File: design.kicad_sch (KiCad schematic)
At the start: 178 parts, among them J1 TYPE-C-31-M-12, U1 TTP223, U10 ATtiny1616-S, U2 TTP223, U3 TTP223, U4 TTP223, U5 TTP223, U6 TTP223, U7 TTP223, U8 TTP223, U9 MAX77751CEFG_T

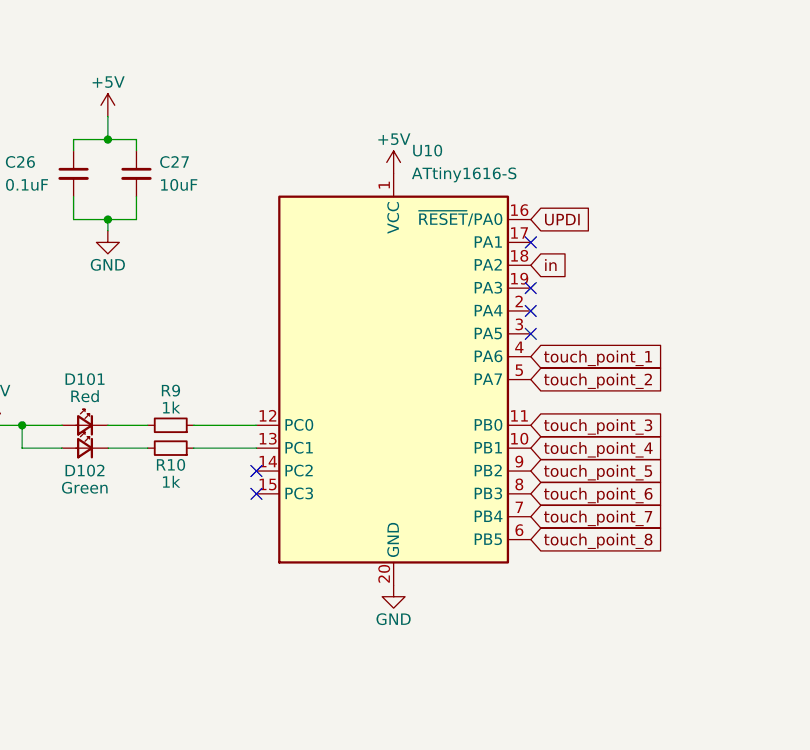
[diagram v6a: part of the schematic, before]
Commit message: change to QFN 1616
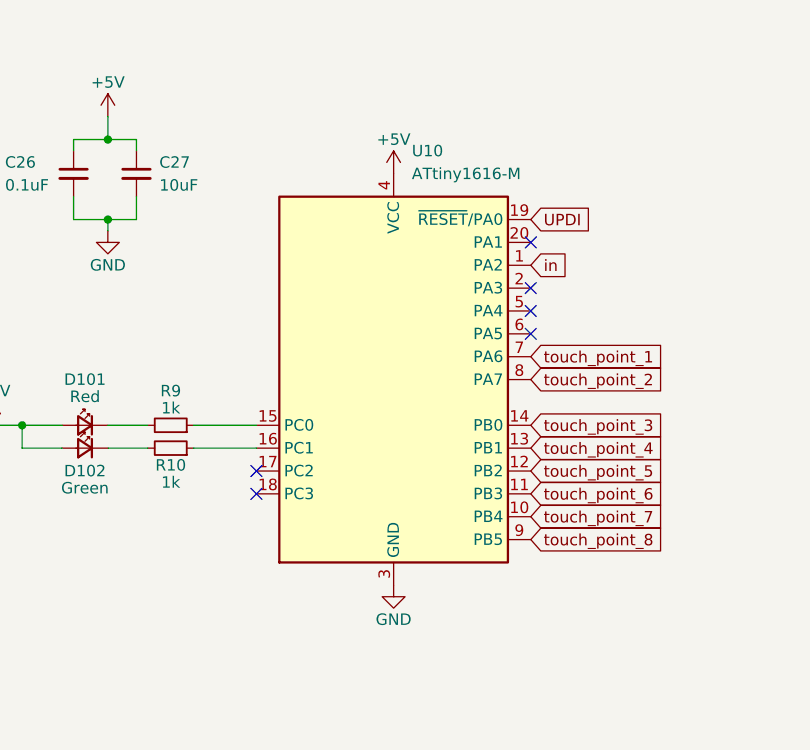
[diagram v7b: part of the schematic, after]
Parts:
- removed U10: ATtiny1616-S, Package_SO:SOIC-20W_7.5x12.8mm_P1.27mm, symbol MCU_Microchip_ATtiny:ATtiny1616-S
- added U10: ATtiny1616-M, Package_DFN_QFN:VQFN-20-1EP_3x3mm_P0.4mm_EP1.7x1.7mm, symbol MCU_Microchip_ATtiny:ATtiny1616-M
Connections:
- net +5V: now also U10.4 (VCC)
- net GND: now also U10.21 (GND), U10.3 (GND)
- net UPDI: now also U10.19 (~{RESET}/PA0)
- net in: now also U10.1 (PA2)
- net touch_point_1: now also U10.7 (PA6)
- net touch_point_2: now also U10.8 (PA7)
- net touch_point_3: now also U10.14 (PB0)
- net touch_point_4: now also U10.13 (PB1)
- net touch_point_5: now also U10.12 (PB2)
- net touch_point_6: now also U10.11 (PB3)
- net touch_point_7: now also U10.10 (PB4)
- net touch_point_8: now also U10.9 (PB5)
- net at R9.1: now also U10.15 (PC0)
- net at R10.1: now also U10.16 (PC1)
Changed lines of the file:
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@@
     (pin "1")
   )
+  (symbol (lib_id "MCU_Microchip_ATtiny:ATtiny1616-M") (at 385.445 314.96 0) (unit 1)
+    (in_bom yes) (on_board yes) (fields_autoplaced)
+    (property "Reference" "U10" (id 0) (at 387.4644 289.56 0)
+      (effects (font (size 1.27 1.27)) (justify left))
+    )
+    (property "Value" "ATtiny1616-M" (id 1) (at 387.4644 292.1 0)
+      (effects (font (size 1.27 1.27)) (justify left))
+    )
+    (property "Footprint" "Package_DFN_QFN:VQFN-20-1EP_3x3mm_P0.4mm_EP1.7x1.7mm" (id 2) (at 385.445 314.96 0)
+      (effects (font (size 1.27 1.27) italic) hide)
+    )
+    (property "Datasheet" "http://ww1.microchip.com/downloads/en/DeviceDoc/ATtiny3216_ATtiny1616-data-sheet-40001997B.pdf" (id 3) (at 385.445 314.96 0)
+      (effects (font (size 1.27 1.27)) hide)
+    )
+    (pin "1")
+    (pin "10")
+    (pin "11")
+    (pin "12")
+    (pin "13")
+    (pin "14")
+    (pin "15")
+    (pin "16")
+    (pin "17")
+    (pin "18")
+    (pin "19")
+    (pin "2")
+    (pin "20")
+    (pin "21")
+    (pin "3")
+    (pin "4")
+    (pin "5")
+    (pin "6")
+    (pin "7")
+    (pin "8")
+    (pin "9")
+  )
   (symbol (lib_id "power:GND") (at 485.14 153.67 0) (unit 1)
     (in_bom yes) (on_board yes)
@@
     (pin "4")
   )
-  (symbol (lib_id "MCU_Microchip_ATtiny:ATtiny1616-S") (at 385.445 314.96 0) (unit 1)
-    (in_bom yes) (on_board yes) (fields_autoplaced)
-    (property "Reference" "U10" (id 0) (at 387.4644 289.56 0)
-      (effects (font (size 1.27 1.27)) (justify left))
-    )
-    (property "Value" "ATtiny1616-S" (id 1) (at 387.4644 292.1 0)
-      (effects (font (size 1.27 1.27)) (justify left))
-    )
-    (property "Footprint" "Package_SO:SOIC-20W_7.5x12.8mm_P1.27mm" (id 2) (at 385.445 314.96 0)
-      (effects (font (size 1.27 1.27) italic) hide)
-    )
-    (property "Datasheet" "http://ww1.microchip.com/downloads/en/DeviceDoc/ATtiny3216_ATtiny1616-data-sheet-40001997B.pdf" (id 3) (at 385.445 314.96 0)
-      (effects (font (size 1.27 1.27)) hide)
-    )
-    (pin "1")
-    (pin "10")
-    (pin "11")
-    (pin "12")
-    (pin "13")
-    (pin "14")
-    (pin "15")
-    (pin "16")
-    (pin "17")
-    (pin "18")
-    (pin "19")
-    (pin "2")
-    (pin "20")
-    (pin "3")
-    (pin "4")
-    (pin "5")
-    (pin "6")
-    (pin "7")
-    (pin "8")
-    (pin "9")
-  )
   (symbol (lib_id "power:GND") (at 551.18 153.67 0) (unit 1)
     (in_bom yes) (on_board yes)
@@
   (symbol (lib_id "power:+5V") (at 196.215 118.11 0) (unit 1)
     (in_bom yes) (on_board yes)
-    (property "Reference" "#PWR?" (id 0) (at 196.215 121.92 0)
+    (property "Reference" "#PWR0256" (id 0) (at 196.215 121.92 0)
       (effects (font (size 1.27 1.27)) hide)
     )
@@
     )
     (path "/e1406b4f-a2c2-4e53-8d5b-e22f2d83d6a5"
-      (reference "#PWR?") (unit 1) (value "+5V") (footprint "")
+      (reference "#PWR0256") (unit 1) (value "+5V") (footprint "")
     )
     (path "/07d1a4e0-733f-4ad9-a5c8-74465e2c313d"
@@
       (reference "U9") (unit 1) (value "MAX77751CEFG_T") (footprint "Snapeda:IC_MAX77751CEFG_T")
     )
-    (path "/a71cdeed-1051-4d62-bd94-dca0a19008a3"
-      (reference "U10") (unit 1) (value "ATtiny1616-S") (footprint "Package_SO:SOIC-20W_7.5x12.8mm_P1.27mm")
+    (path "/06824c68-cecd-4391-bdbb-9ca63f76c08e"
+      (reference "U10") (unit 1) (value "ATtiny1616-M") (footprint "Package_DFN_QFN:VQFN-20-1EP_3x3mm_P0.4mm_EP1.7x1.7mm")
     )
   )

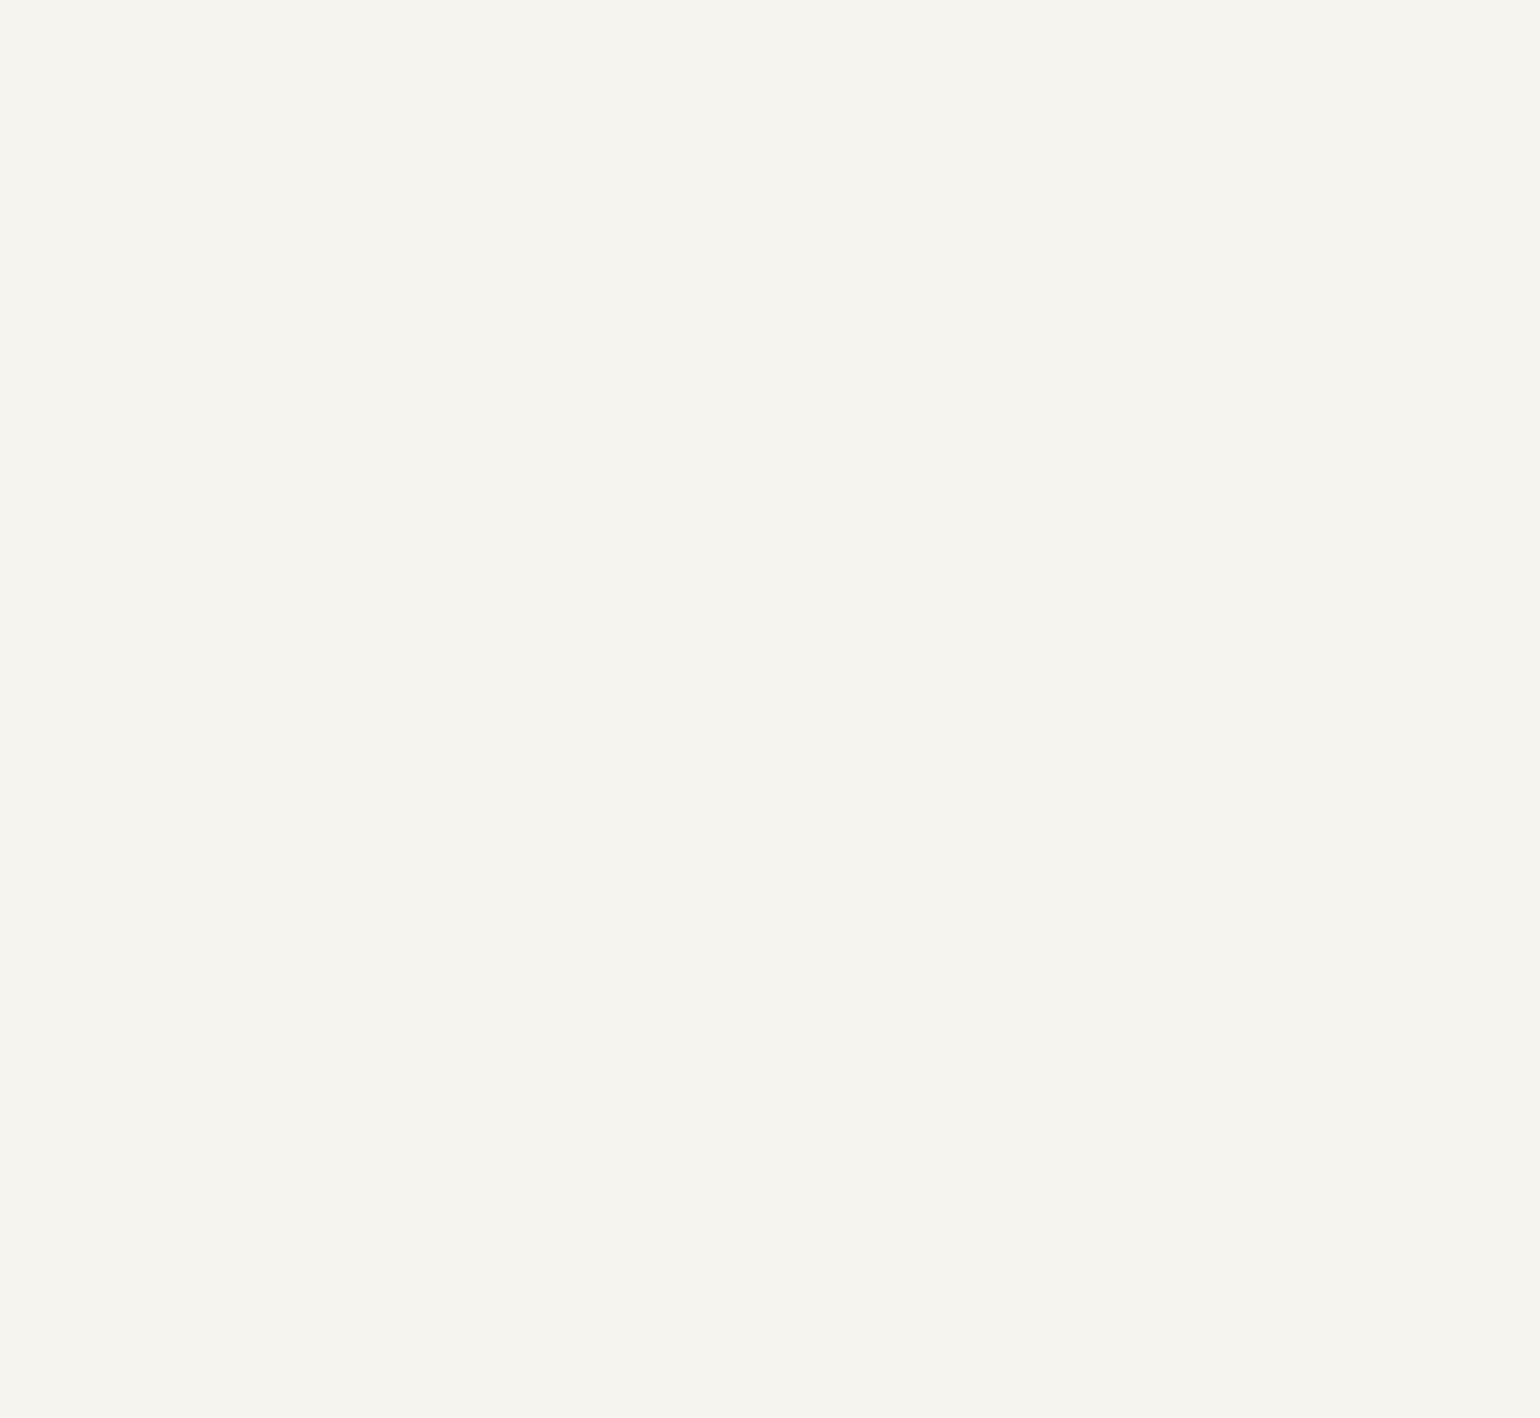
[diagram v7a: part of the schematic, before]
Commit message: some confusing LED double footprints
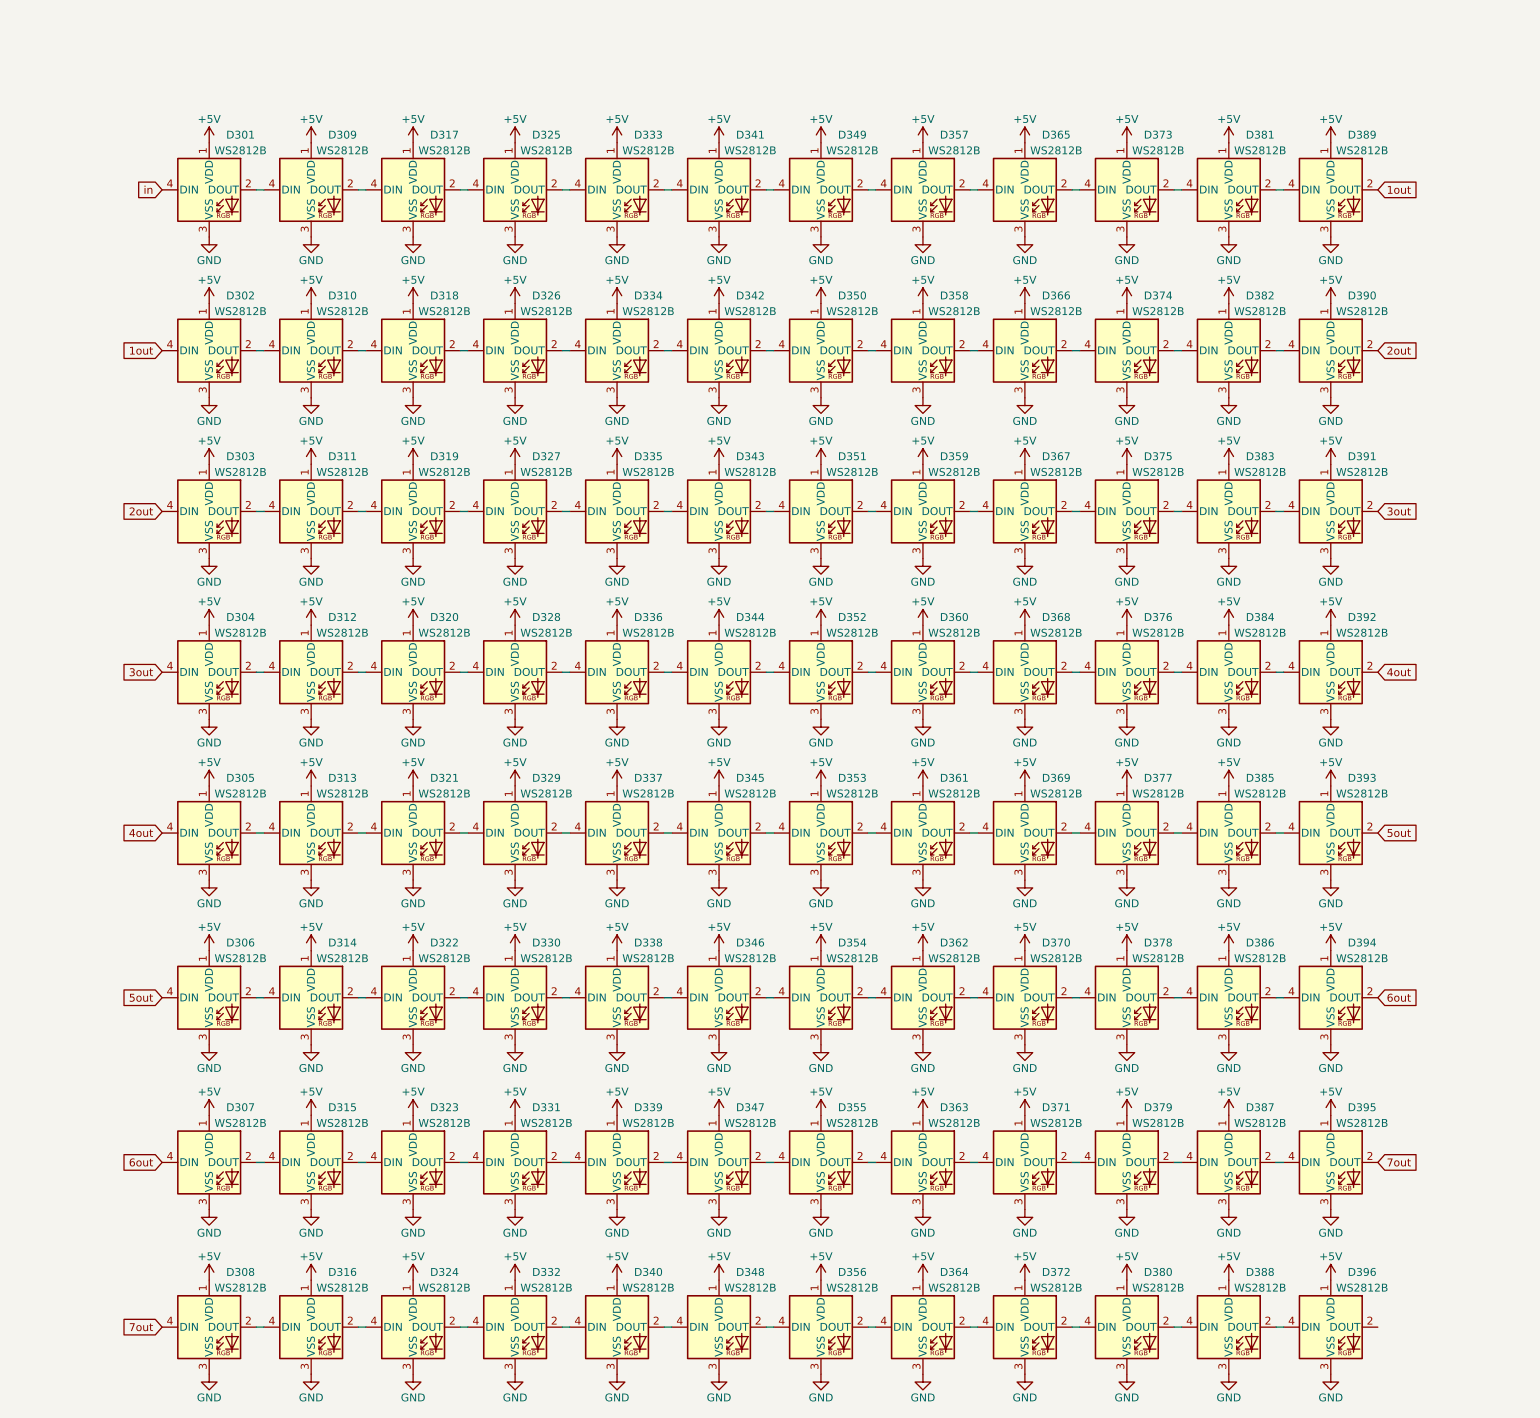
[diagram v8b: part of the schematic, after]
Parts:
- added D301, D302, D303, D304, D305, D306, D307, D308, D309, D310, D311, D312, D313, D314, D315, D316, D317, D318, D319, D320, D321, D322, D323, D324, D325, D326, D327, D328, D329, D330, D331, D332, D333, D334, D335, D336, D337, D338, D339, D340, D341, D342, D343, D344, D345, D346, D347, D348, D349, D350, D351, D352, D353, D354, D355, D356, D357, D358, D359, D360, D361, D362, D363, D364, D365, D366, D367, D368, D369, D370, D371, D372, D373, D374, D375, D376, D377, D378, D379, D380, D381, D382, D383, D384, D385, D386, D387, D388, D389, D390, D391, D392, D393, D394, D395, D396: WS2812B, LED_SMD:LED_WS2812B_PLCC4_5.0x5.0mm_P3.2mm, symbol LED:WS2812B
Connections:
- net +5V: now also D301.1 (VDD), D302.1 (VDD), D303.1 (VDD), D304.1 (VDD), D305.1 (VDD), D306.1 (VDD), D307.1 (VDD), D308.1 (VDD), D309.1 (VDD), D310.1 (VDD), D311.1 (VDD), D312.1 (VDD), D313.1 (VDD), D314.1 (VDD), D315.1 (VDD), D316.1 (VDD), D317.1 (VDD), D318.1 (VDD), D319.1 (VDD), D320.1 (VDD), D321.1 (VDD), D322.1 (VDD), D323.1 (VDD), D324.1 (VDD), D325.1 (VDD), D326.1 (VDD), D327.1 (VDD), D328.1 (VDD), D329.1 (VDD), D330.1 (VDD), D331.1 (VDD), D332.1 (VDD), D333.1 (VDD), D334.1 (VDD), D335.1 (VDD), D336.1 (VDD), D337.1 (VDD), D338.1 (VDD), D339.1 (VDD), D340.1 (VDD), D341.1 (VDD), D342.1 (VDD), D343.1 (VDD), D344.1 (VDD), D345.1 (VDD), D346.1 (VDD), D347.1 (VDD), D348.1 (VDD), D349.1 (VDD), D350.1 (VDD), D351.1 (VDD), D352.1 (VDD), D353.1 (VDD), D354.1 (VDD), D355.1 (VDD), D356.1 (VDD), D357.1 (VDD), D358.1 (VDD), D359.1 (VDD), D360.1 (VDD), D361.1 (VDD), D362.1 (VDD), D363.1 (VDD), D364.1 (VDD), D365.1 (VDD), D366.1 (VDD), D367.1 (VDD), D368.1 (VDD), D369.1 (VDD), D370.1 (VDD), D371.1 (VDD), D372.1 (VDD), D373.1 (VDD), D374.1 (VDD), D375.1 (VDD), D376.1 (VDD), D377.1 (VDD), D378.1 (VDD), D379.1 (VDD), D380.1 (VDD), D381.1 (VDD), D382.1 (VDD), D383.1 (VDD), D384.1 (VDD), D385.1 (VDD), D386.1 (VDD), D387.1 (VDD), D388.1 (VDD), D389.1 (VDD), D390.1 (VDD), D391.1 (VDD), D392.1 (VDD), D393.1 (VDD), D394.1 (VDD), D395.1 (VDD), D396.1 (VDD)
- net 1out: now also D302.4 (DIN), D389.2 (DOUT)
- net 2out: now also D303.4 (DIN), D390.2 (DOUT)
- net 3out: now also D304.4 (DIN), D391.2 (DOUT)
- net 4out: now also D305.4 (DIN), D392.2 (DOUT)
- net 5out: now also D306.4 (DIN), D393.2 (DOUT)
- net 6out: now also D307.4 (DIN), D394.2 (DOUT)
- net 7out: now also D308.4 (DIN), D395.2 (DOUT)
- net GND: now also D301.3 (VSS), D302.3 (VSS), D303.3 (VSS), D304.3 (VSS), D305.3 (VSS), D306.3 (VSS), D307.3 (VSS), D308.3 (VSS), D309.3 (VSS), D310.3 (VSS), D311.3 (VSS), D312.3 (VSS), D313.3 (VSS), D314.3 (VSS), D315.3 (VSS), D316.3 (VSS), D317.3 (VSS), D318.3 (VSS), D319.3 (VSS), D320.3 (VSS), D321.3 (VSS), D322.3 (VSS), D323.3 (VSS), D324.3 (VSS), D325.3 (VSS), D326.3 (VSS), D327.3 (VSS), D328.3 (VSS), D329.3 (VSS), D330.3 (VSS), D331.3 (VSS), D332.3 (VSS), D333.3 (VSS), D334.3 (VSS), D335.3 (VSS), D336.3 (VSS), D337.3 (VSS), D338.3 (VSS), D339.3 (VSS), D340.3 (VSS), D341.3 (VSS), D342.3 (VSS), D343.3 (VSS), D344.3 (VSS), D345.3 (VSS), D346.3 (VSS), D347.3 (VSS), D348.3 (VSS), D349.3 (VSS), D350.3 (VSS), D351.3 (VSS), D352.3 (VSS), D353.3 (VSS), D354.3 (VSS), D355.3 (VSS), D356.3 (VSS), D357.3 (VSS), D358.3 (VSS), D359.3 (VSS), D360.3 (VSS), D361.3 (VSS), D362.3 (VSS), D363.3 (VSS), D364.3 (VSS), D365.3 (VSS), D366.3 (VSS), D367.3 (VSS), D368.3 (VSS), D369.3 (VSS), D370.3 (VSS), D371.3 (VSS), D372.3 (VSS), D373.3 (VSS), D374.3 (VSS), D375.3 (VSS), D376.3 (VSS), D377.3 (VSS), D378.3 (VSS), D379.3 (VSS), D380.3 (VSS), D381.3 (VSS), D382.3 (VSS), D383.3 (VSS), D384.3 (VSS), D385.3 (VSS), D386.3 (VSS), D387.3 (VSS), D388.3 (VSS), D389.3 (VSS), D390.3 (VSS), D391.3 (VSS), D392.3 (VSS), D393.3 (VSS), D394.3 (VSS), D395.3 (VSS), D396.3 (VSS)
- net in: now also D301.4 (DIN)
- new net: D367.2 (DOUT), D375.4 (DIN)
- new net: D359.2 (DOUT), D367.4 (DIN)
- new net: D332.2 (DOUT), D340.4 (DIN)
- new net: D324.2 (DOUT), D332.4 (DIN)
- new net: D327.2 (DOUT), D335.4 (DIN)
- new net: D319.2 (DOUT), D327.4 (DIN)
- new net: D302.2 (DOUT), D310.4 (DIN)
- new net: D328.2 (DOUT), D336.4 (DIN)
- new net: D320.2 (DOUT), D328.4 (DIN)
- new net: D352.2 (DOUT), D360.4 (DIN)
- new net: D344.2 (DOUT), D352.4 (DIN)
- new net: D375.2 (DOUT), D383.4 (DIN)
- new net: D351.2 (DOUT), D359.4 (DIN)
- new net: D305.2 (DOUT), D313.4 (DIN)
- new net: D360.2 (DOUT), D368.4 (DIN)
- new net: D338.2 (DOUT), D346.4 (DIN)
- new net: D330.2 (DOUT), D338.4 (DIN)
- new net: D311.2 (DOUT), D319.4 (DIN)
- new net: D303.2 (DOUT), D311.4 (DIN)
- new net: D333.2 (DOUT), D341.4 (DIN)
- new net: D325.2 (DOUT), D333.4 (DIN)
- new net: D343.2 (DOUT), D351.4 (DIN)
- new net: D335.2 (DOUT), D343.4 (DIN)
- new net: D301.2 (DOUT), D309.4 (DIN)
- new net: D384.2 (DOUT), D392.4 (DIN)
- new net: D376.2 (DOUT), D384.4 (DIN)
- new net: D365.2 (DOUT), D373.4 (DIN)
- new net: D357.2 (DOUT), D365.4 (DIN)
- new net: D354.2 (DOUT), D362.4 (DIN)
- new net: D346.2 (DOUT), D354.4 (DIN)
- new net: D339.2 (DOUT), D347.4 (DIN)
- new net: D331.2 (DOUT), D339.4 (DIN)
- new net: D345.2 (DOUT), D353.4 (DIN)
- new net: D337.2 (DOUT), D345.4 (DIN)
- new net: D386.2 (DOUT), D394.4 (DIN)
- new net: D316.2 (DOUT), D324.4 (DIN)
- new net: D315.2 (DOUT), D323.4 (DIN)
- new net: D307.2 (DOUT), D315.4 (DIN)
- new net: D382.2 (DOUT), D390.4 (DIN)
- new net: D374.2 (DOUT), D382.4 (DIN)
- new net: D387.2 (DOUT), D395.4 (DIN)
- new net: D379.2 (DOUT), D387.4 (DIN)
- new net: D361.2 (DOUT), D369.4 (DIN)
- new net: D353.2 (DOUT), D361.4 (DIN)
- new net: D329.2 (DOUT), D337.4 (DIN)
- new net: D321.2 (DOUT), D329.4 (DIN)
- new net: D378.2 (DOUT), D386.4 (DIN)
- new net: D370.2 (DOUT), D378.4 (DIN)
- new net: D334.2 (DOUT), D342.4 (DIN)
- new net: D326.2 (DOUT), D334.4 (DIN)
- new net: D364.2 (DOUT), D372.4 (DIN)
- new net: D356.2 (DOUT), D364.4 (DIN)
- new net: D385.2 (DOUT), D393.4 (DIN)
- new net: D377.2 (DOUT), D385.4 (DIN)
- new net: D308.2 (DOUT), D316.4 (DIN)
- new net: D383.2 (DOUT), D391.4 (DIN)
- new net: D373.2 (DOUT), D381.4 (DIN)
- new net: D380.2 (DOUT), D388.4 (DIN)
- new net: D372.2 (DOUT), D380.4 (DIN)
- new net: D322.2 (DOUT), D330.4 (DIN)
- new net: D347.2 (DOUT), D355.4 (DIN)
- new net: D314.2 (DOUT), D322.4 (DIN)
- new net: D306.2 (DOUT), D314.4 (DIN)
- new net: D341.2 (DOUT), D349.4 (DIN)
- new net: D313.2 (DOUT), D321.4 (DIN)
- new net: D358.2 (DOUT), D366.4 (DIN)
- new net: D350.2 (DOUT), D358.4 (DIN)
- new net: D312.2 (DOUT), D320.4 (DIN)
- new net: D304.2 (DOUT), D312.4 (DIN)
- new net: D336.2 (DOUT), D344.4 (DIN)
- new net: D388.2 (DOUT), D396.4 (DIN)
- new net: D366.2 (DOUT), D374.4 (DIN)
- new net: D342.2 (DOUT), D350.4 (DIN)
- new net: D349.2 (DOUT), D357.4 (DIN)
- new net: D369.2 (DOUT), D377.4 (DIN)
- new net: D362.2 (DOUT), D370.4 (DIN)
- new net: D310.2 (DOUT), D318.4 (DIN)
- new net: D368.2 (DOUT), D376.4 (DIN)
- new net: D323.2 (DOUT), D331.4 (DIN)
- new net: D317.2 (DOUT), D325.4 (DIN)
- new net: D363.2 (DOUT), D371.4 (DIN)
- new net: D355.2 (DOUT), D363.4 (DIN)
- new net: D371.2 (DOUT), D379.4 (DIN)
- new net: D309.2 (DOUT), D317.4 (DIN)
- new net: D381.2 (DOUT), D389.4 (DIN)
- new net: D318.2 (DOUT), D326.4 (DIN)
- new net: D348.2 (DOUT), D356.4 (DIN)
- new net: D340.2 (DOUT), D348.4 (DIN)
